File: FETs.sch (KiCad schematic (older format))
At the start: 20 parts, among them Q1 CSD18531Q5A, Q2 CSD18531Q5A, Q3 CSD18531Q5A, Q4 CSD18531Q5A, Q5 CSD18531Q5A, Q6 CSD18531Q5A, Q7 CSD18531Q5A, Q8 CSD18531Q5A

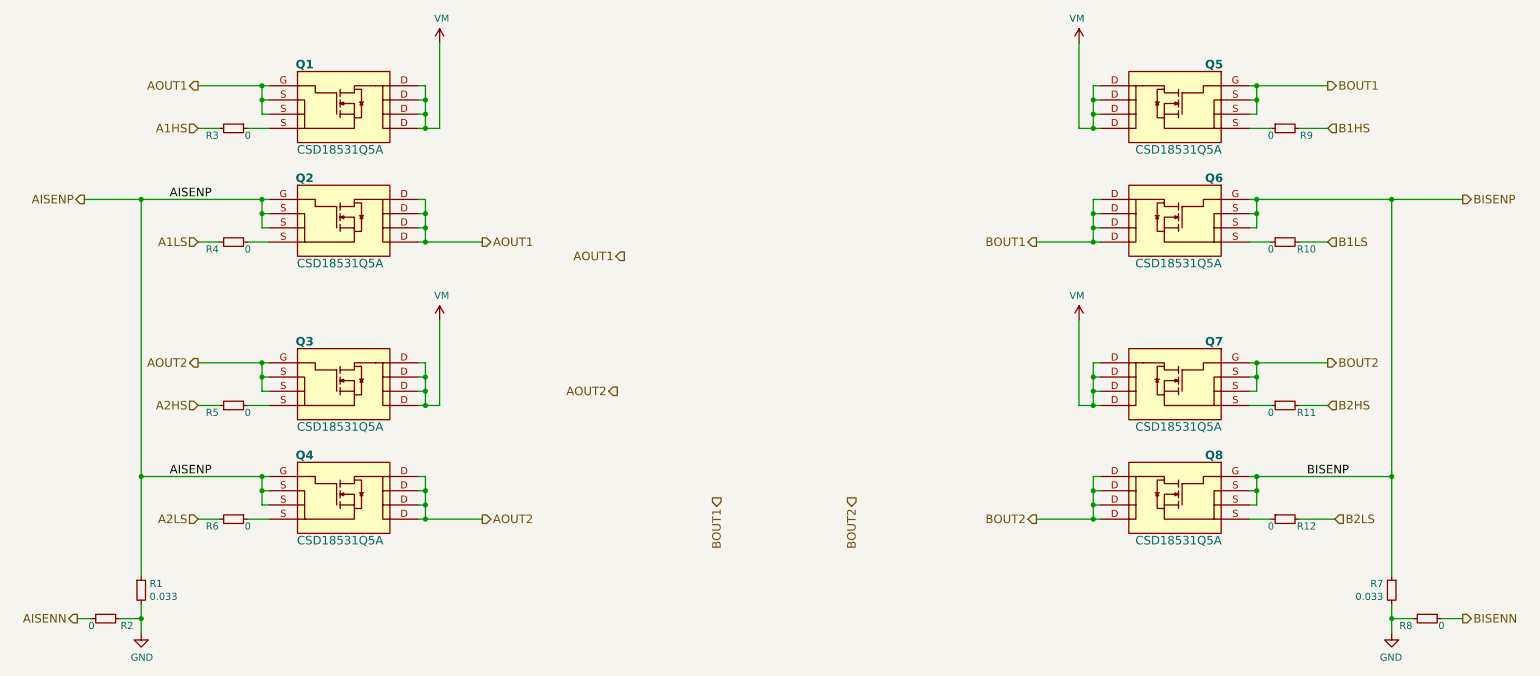
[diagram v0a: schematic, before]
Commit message: adding decoupling filters
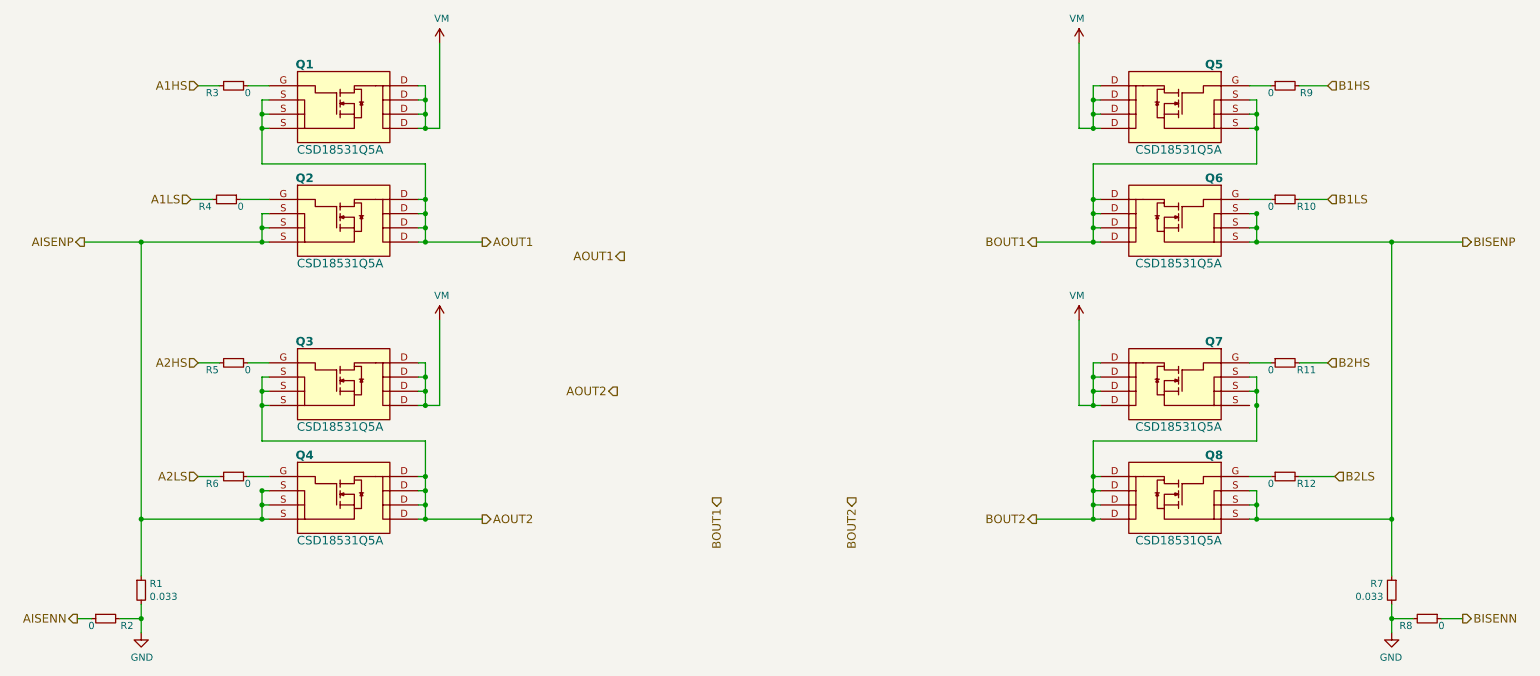
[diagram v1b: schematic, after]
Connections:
- net AISENP: no longer Q2.G, Q4.G
- net AOUT1: no longer Q1.G
- net AOUT2: no longer Q3.G
- net BISENP: no longer Q6.G, Q8.G
- net BOUT1: no longer Q5.G
- net BOUT2: no longer Q7.G
- net at R3.1: now also Q1.G; no longer Q1.S
- net at R4.1: now also Q2.G; no longer Q2.S
- net at R9.1: now also Q5.G; no longer Q5.S
- net at R10.1: now also Q6.G; no longer Q6.S
- net at R5.1: now also Q3.G; no longer Q3.S
- net at R6.1: now also Q4.G; no longer Q4.S
- net at R11.1: now also Q7.G; no longer Q7.S
- net at R12.1: now also Q8.G; no longer Q8.S
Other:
- moved on the sheet: R10, R11, R12, R3, R4, R5, R6, R9
